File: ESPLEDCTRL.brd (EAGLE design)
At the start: 102.5 x 80 mm, 5 parts, among them J1 22-27-2031-03, X3 ZX62D-B-5PA8

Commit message: Eine Diode
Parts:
- added D1: 1N4148DO35-7, diode:DO35-7
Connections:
- new net N$2: D1.C, U$1.JP2.8
- net VCC: now also D1.A; no longer U$1.JP2.8
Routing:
- net VCC: track 118.5 -> 69.4 mm
- net N$2: track 0.00 -> 49.0 mm
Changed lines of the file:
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@@
 <?xml version="1.0" encoding="utf-8"?>
 <!DOCTYPE eagle SYSTEM "eagle.dtd">
-<eagle version="9.5.1">
+<eagle version="8.7.1">
 <drawing>
 <settings>
@@
 <param name="checkStop" value="0"/>
 <param name="checkValues" value="0"/>
-<param name="checkNames" value="1"/>
-<param name="checkWireStubs" value="1"/>
-<param name="checkPolygonWidth" value="0"/>
 <param name="useDiameter" value="13"/>
 <param name="maxErrors" value="50"/>
@@
 <attribute name="VALUE" x="65.5589" y="59.7169" size="0.8128" layer="27" ratio="10" rot="R90"/>
 </element>
+<element name="D1" library="diode" library_urn="urn:adsk.eagle:library:210" package="DO35-7" package3d_urn="urn:adsk.eagle:package:43339/1" value="1N4148DO35-7" x="6.35" y="-7.62"/>
 </elements>
 <signals>
@@
 <signal name="VCC">
 <contactref element="X3" pad="1"/>
-<contactref element="U$1" pad="JP2.8"/>
 <wire x1="36.2712" y1="62.3316" x2="10.668" y2="62.3316" width="0.1524" layer="1"/>
 <wire x1="10.668" y1="62.3316" x2="8.6868" y2="62.3316" width="0.1524" layer="1"/>
 <wire x1="39.9288" y1="65.9892" x2="36.2712" y2="62.3316" width="0.1524" layer="1"/>
 <wire x1="8.6868" y1="62.3316" x2="8.635" y2="62.26" width="0.1524" layer="1"/>
-<wire x1="39.9288" y1="65.9892" x2="40.005" y2="66.04" width="0.1524" layer="1"/>
-<wire x1="40.0812" y1="65.9892" x2="59.1312" y2="65.9892" width="0.1524" layer="1"/>
-<wire x1="59.1312" y1="65.9892" x2="60.96" y2="65.9892" width="0.1524" layer="1"/>
-<wire x1="40.0812" y1="65.9892" x2="40.005" y2="66.04" width="0.1524" layer="1"/>
 <wire x1="5.334" y1="31.242" x2="7.62" y2="28.956" width="0.1524" layer="1"/>
 <wire x1="5.334" y1="52.2732" x2="5.334" y2="31.242" width="0.1524" layer="1"/>
 <wire x1="10.668" y1="57.6072" x2="5.334" y2="52.2732" width="0.1524" layer="1"/>
 <wire x1="10.668" y1="62.3316" x2="10.668" y2="57.6072" width="0.1524" layer="1"/>
-<wire x1="59.5884" y1="60.0456" x2="59.5884" y2="38.1" width="0.1524" layer="1"/>
-<wire x1="59.1312" y1="60.5028" x2="59.5884" y2="60.0456" width="0.1524" layer="1"/>
-<wire x1="59.1312" y1="65.9892" x2="59.1312" y2="60.5028" width="0.1524" layer="1"/>
-<contactref element="X2" pad="1"/>
 <contactref element="X1" pad="1"/>
 <contactref element="J1" pad="1"/>
-<wire x1="60.96" y1="65.9892" x2="60.96" y2="66.04" width="0" layer="19" extent="1-1"/>
-<wire x1="59.69" y1="38.0746" x2="59.5884" y2="38.1" width="0" layer="19" extent="1-1"/>
+<contactref element="X2" pad="1"/>
+<contactref element="D1" pad="A"/>
+<wire x1="39.9288" y1="65.9892" x2="60.96" y2="66.04" width="0" layer="19" extent="1-1"/>
 <wire x1="7.62" y1="26.6954" x2="7.62" y2="28.956" width="0" layer="19" extent="1-1"/>
+<wire x1="59.69" y1="38.0746" x2="60.96" y2="66.04" width="0" layer="19" extent="1-1"/>
+<wire x1="10.16" y1="-7.62" x2="7.62" y2="26.6954" width="0" layer="19" extent="1-1"/>
 </signal>
 <signal name="N$1">
@@
 <wire x1="60.96" y1="63.5508" x2="60.96" y2="63.5" width="0.1524" layer="16"/>
 </signal>
+<signal name="N$2">
+<contactref element="U$1" pad="JP2.8"/>
+<contactref element="D1" pad="C"/>
+<wire x1="40.0812" y1="65.9892" x2="59.1312" y2="65.9892" width="0.1524" layer="1"/>
+<wire x1="59.1312" y1="65.9892" x2="60.96" y2="65.9892" width="0.1524" layer="1"/>
+<wire x1="40.0812" y1="65.9892" x2="40.005" y2="66.04" width="0.1524" layer="1"/>
+<wire x1="59.5884" y1="60.0456" x2="59.5884" y2="38.1" width="0.1524" layer="1"/>
+<wire x1="59.1312" y1="60.5028" x2="59.5884" y2="60.0456" width="0.1524" layer="1"/>
+<wire x1="59.1312" y1="65.9892" x2="59.1312" y2="60.5028" width="0.1524" layer="1"/>
+<wire x1="2.54" y1="-7.62" x2="59.5884" y2="38.1" width="0" layer="19" extent="1-1"/>
+</signal>
 </signals>
-<mfgpreviewcolors>
-<mfgpreviewcolor name="soldermaskcolor" color="0xC8008000"/>
-<mfgpreviewcolor name="silkscreencolor" color="0xFFFEFEFE"/>
-<mfgpreviewcolor name="backgroundcolor" color="0xFF282828"/>
-<mfgpreviewcolor name="coppercolor" color="0xFFFFBF00"/>
-<mfgpreviewcolor name="substratecolor" color="0xFF786E46"/>
-</mfgpreviewcolors>
 </board>
 </drawing>

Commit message: Die Diode
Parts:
- moved D1 36.6 mm to (26.7, 22.9), turned to 180 degrees
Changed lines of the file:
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@@
 <attribute name="VALUE" x="65.5589" y="59.7169" size="0.8128" layer="27" ratio="10" rot="R90"/>
 </element>
-<element name="D1" library="diode" library_urn="urn:adsk.eagle:library:210" package="DO35-7" package3d_urn="urn:adsk.eagle:package:43339/1" value="1N4148DO35-7" x="6.35" y="-7.62"/>
+<element name="D1" library="diode" library_urn="urn:adsk.eagle:library:210" package="DO35-7" package3d_urn="urn:adsk.eagle:package:43339/1" value="1N4148DO35-7" x="26.67" y="22.86" rot="R180"/>
 </elements>
 <signals>
@@
 <wire x1="7.62" y1="26.6954" x2="7.62" y2="28.956" width="0" layer="19" extent="1-1"/>
 <wire x1="59.69" y1="38.0746" x2="60.96" y2="66.04" width="0" layer="19" extent="1-1"/>
-<wire x1="10.16" y1="-7.62" x2="7.62" y2="26.6954" width="0" layer="19" extent="1-1"/>
+<wire x1="22.86" y1="22.86" x2="7.62" y2="26.6954" width="0" layer="19" extent="1-1"/>
 </signal>
 <signal name="N$1">
@@
 <wire x1="59.1312" y1="60.5028" x2="59.5884" y2="60.0456" width="0.1524" layer="1"/>
 <wire x1="59.1312" y1="65.9892" x2="59.1312" y2="60.5028" width="0.1524" layer="1"/>
-<wire x1="2.54" y1="-7.62" x2="59.5884" y2="38.1" width="0" layer="19" extent="1-1"/>
+<wire x1="30.48" y1="22.86" x2="59.5884" y2="38.1" width="0" layer="19" extent="1-1"/>
 </signal>
 </signals>

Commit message: some changes
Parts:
- moved D1 47.1 mm to (30.5, 69.8)
- moved X1 5.24 mm to (8.89, 34.3)
- moved J1 4.02 mm to (59.7, 59.7)
- moved X2 2.84 mm to (57.1, 34.3)
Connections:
- net VCC renamed N$3
- new net N$4: J1.3, X1.2, X2.2
- net GND: no longer J1.3, X1.2, X2.2, X3.5
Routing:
- net GND: track 146.9 -> 0.00 mm
- net N$4: track 0.00 -> 76.8 mm
- net N$3: track 69.4 -> 115.9 mm
- net N$2: track 49.0 -> 7.33 mm
- net N$1: track 28.0 -> 30.0 mm

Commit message: Alte Version
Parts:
- added J2: 22-27-2041-04, con-molex:6410-04
- added JP1: (no value), jumper:JP5Q
- added S1: (no value), switch-omron:B3F-10XX
- added SV1: (no value), con-lstb:MA03-1
- added X4: MINI-USB-32005-201, con-cypressindustries:32005-201
- moved D1 62.7 mm to (22.9, 7.62), turned to 270 degrees
- moved X2 33.8 mm to (76.2, 6.35), turned to 90 degrees
- moved J1 33.5 mm to (73.7, 29.2)
- moved U$1 32.6 mm to (43.2, 24.1), turned to 270 degrees
- moved X1 28.0 mm to (7.62, 6.35)
- moved X3 26.7 mm to (3.81, 34.3)
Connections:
- removed net 3V3: U$1.JP1.8
- new net N$10: J2.3, U$1.JP1.2
- new net N$11: J1.3, J2.1, JP1.10, JP1.2, JP1.4, JP1.6, JP1.8, S1.3, X1.2, X2.2, X3.5, X4.5
- new net N$12: J2.4, U$1.JP1.8
- new net N$13: D1.A, J1.1, SV1.1, X1.1, X2.1, X3.1, X4.1
- new net N$14: SV1.3, X3.3
- new net N$5: JP1.1, U$1.JP2.4
- new net N$6: J2.2, U$1.JP1.1
- new net N$7: JP1.3, U$1.JP2.3
- new net N$8: JP1.5, U$1.JP2.2
- new net N$9: JP1.7, U$1.JP2.1
- net N$3: now also SV1.2, X3.2; no longer D1.A, J1.1, X1.1, X2.1, X3.1
- net N$4: now also JP1.9, S1.1, U$1.JP2.5; no longer J1.3, X1.2, X2.2
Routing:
- net N$3: track 115.9 -> 0.00 mm
- net N$4: track 76.8 -> 0.00 mm
- net N$1: track 30.0 -> 0.00 mm
- net N$2: track 7.33 -> 0.00 mm
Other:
- board size 102.5 x 80 mm -> 83.5 x 43.2 mm

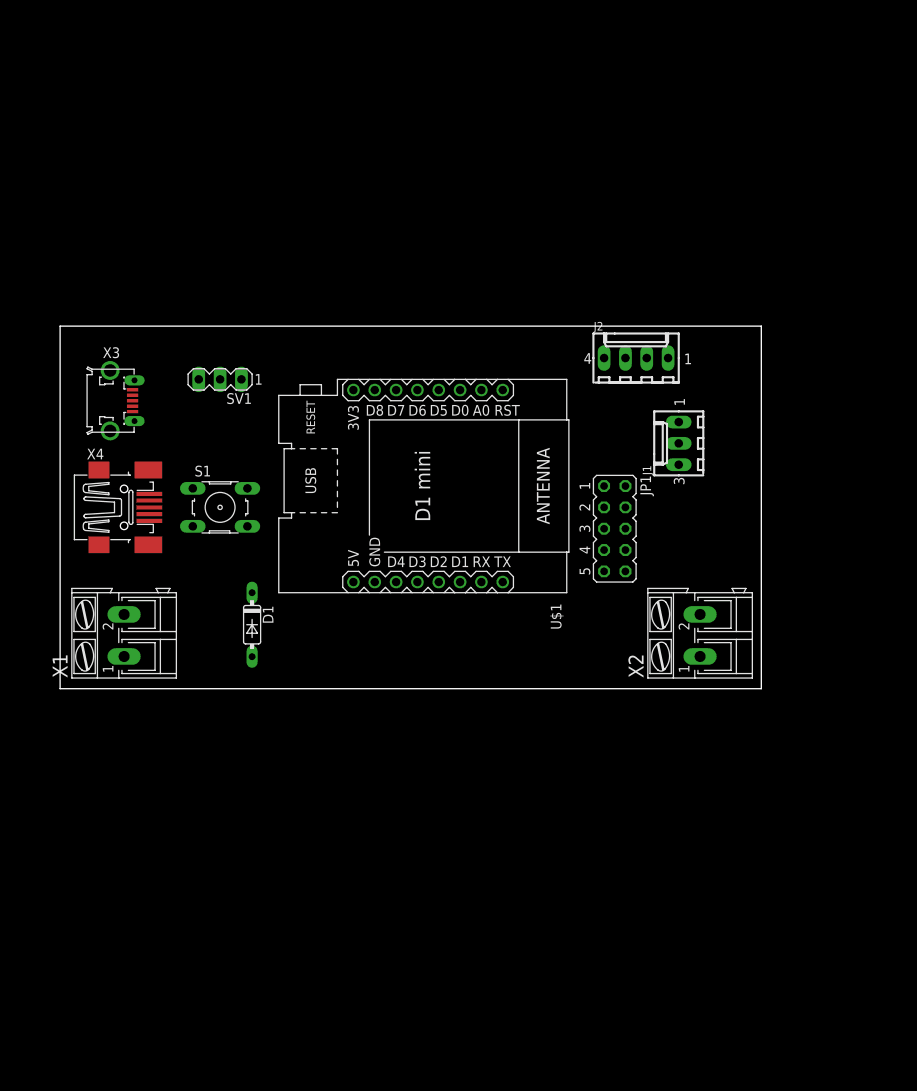
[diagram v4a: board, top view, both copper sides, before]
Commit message: Umbau auf Version 2 beginnt
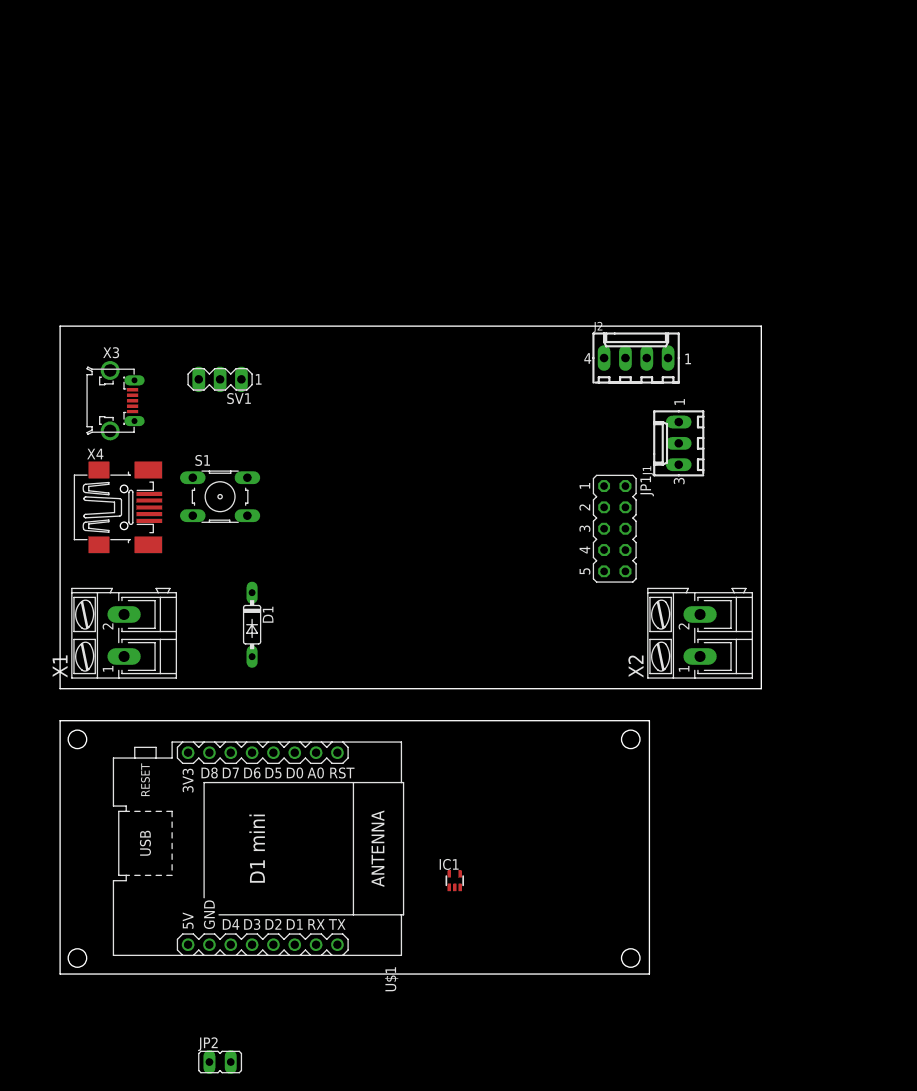
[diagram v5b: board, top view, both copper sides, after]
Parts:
- added IC1: 74HC1G08GW, Logik-IC:SOT353
- added JP2: (no value), jumper:JP1
- moved U$1 47.5 mm to (23.5, -19.1)
- moved S1 1.27 mm to (19.1, 22.9)
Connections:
- new net +5V: IC1.5, U$1.JP2.8
- new net 3V3: U$1.JP1.8
- new net N$15: U$1.JP2.6
- new net N$16: IC1.1, IC1.2, U$1.JP2.2
- new net N$18: IC1.4
- net GND: now also IC1.3, JP2.1
- net N$1: now also JP2.2, U$1.JP2.5; no longer J1.2, U$1.JP2.6
- net N$10: no longer U$1.JP1.2
- net N$12: no longer U$1.JP1.8
- net N$2: no longer U$1.JP2.8
- net N$4: no longer U$1.JP2.5
- net N$5: no longer U$1.JP2.4
- net N$6: no longer U$1.JP1.1
- net N$7: no longer U$1.JP2.3
- net N$8: no longer U$1.JP2.2
- net N$9: no longer U$1.JP2.1
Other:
- board size 83.5 x 43.2 mm -> 83.5 x 77.1 mm

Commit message: Leiterplatte Anordnung vorbereitet DCDC wandler ist 14mm hoch
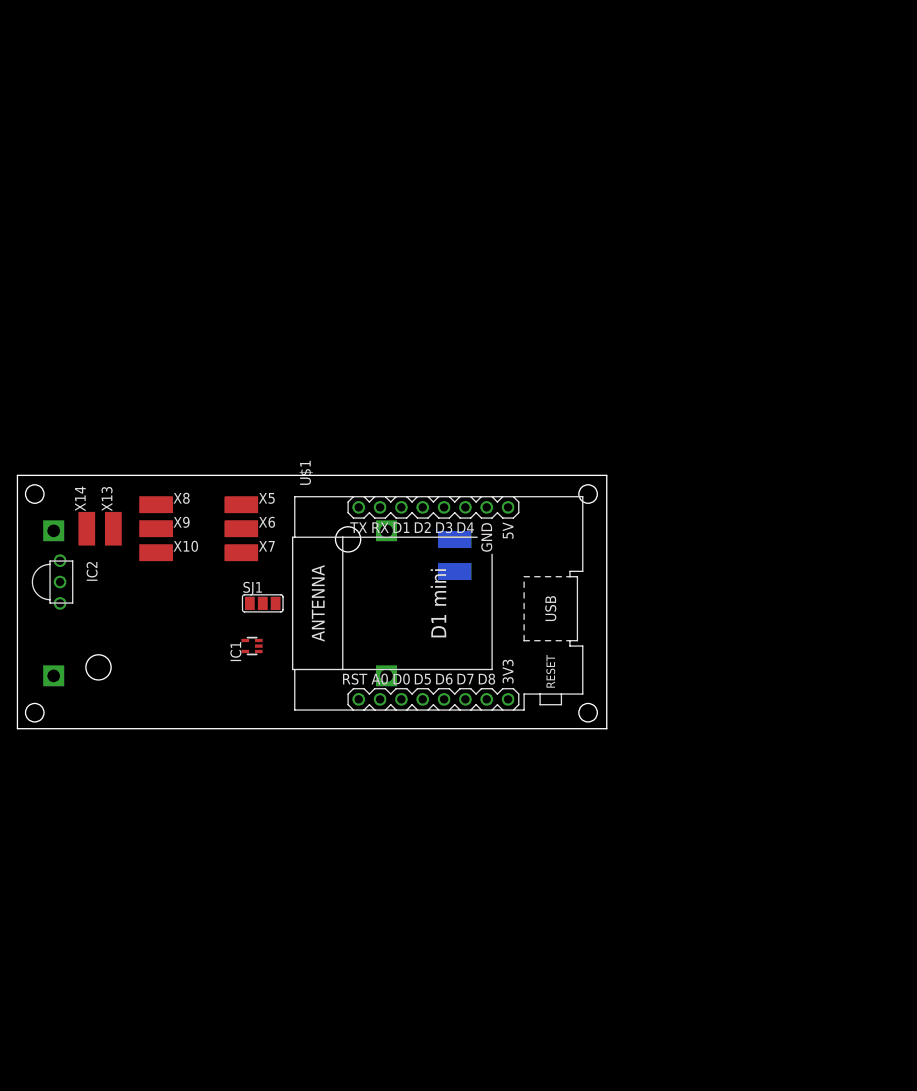
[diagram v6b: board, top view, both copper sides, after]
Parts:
- removed D1: 1N4148DO35-7, diode:DO35-7
- removed J1: 22-27-2031-03, con-molex:6410-03
- removed J2: 22-27-2041-04, con-molex:6410-04
- removed JP1: (no value), jumper:JP5Q
- removed JP2: (no value), jumper:JP1
- removed S1: (no value), switch-omron:B3F-10XX
- removed SV1: (no value), con-lstb:MA03-1
- removed X1, X2: (no value), con-ptr500:AK300/2
- removed X3: ZX62D-B-5PA8, zx62d-b-5pa8-oshpark_10:ZX62D-B-5PA8
- removed X4: MINI-USB-32005-201, con-cypressindustries:32005-201
- added IC2: (no value), modules:TSOP38
- added SJ1: (no value), jumper:SJ_2
- added U$2: DC-DC-STEP-DOWN-LM2596, diy-modules:DC-DC-STEP-DOWN-LM2596
- added X10, X11, X12, X13, X14, X5, X6, X7, X8, X9: (no value), modules:PAD2X4
- moved IC1 36.9 mm to (22.9, 5.08), turned to 90 degrees
- moved U$1 36.3 mm to (45.1, 10.2), turned to 90 degrees
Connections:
- removed net N$10: J2.3
- removed net N$11: J1.3, J2.1, JP1.10, JP1.2, JP1.4, JP1.6, JP1.8, S1.3, X1.2, X2.2, X3.5, X4.5
- removed net N$12: J2.4
- removed net N$13: D1.A, J1.1, SV1.1, X1.1, X2.1, X3.1, X4.1
- removed net N$14: SV1.3, X3.3
- removed net N$3: SV1.2, X3.2
- removed net N$4: JP1.9, S1.1
- removed net N$5: JP1.1
- removed net N$6: J2.2
- removed net N$7: JP1.3
- removed net N$8: JP1.5
- removed net N$9: JP1.7
- new net N$17: SJ1.3, U$1.JP1.3
- new net N$21: U$2.IN+, X11.P$1
- net +5V: now also IC2.3, U$2.OUT+, X5.P$1, X8.P$1
- net GND: now also IC2.2, U$2.IN-, U$2.OUT-, X10.P$1, X12.P$1, X14.P$1, X7.P$1; no longer JP2.1
- net N$1: now also X13.P$1; no longer JP2.2
- net N$15: now also SJ1.1
- net N$16: now also SJ1.2; no longer U$1.JP2.2
- net N$18: now also X6.P$1
- net N$2: now also IC2.1, U$1.JP2.4; no longer D1.C
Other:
- board size 83.5 x 77.1 mm -> 70.2 x 30.2 mm

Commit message: Board fertig gestellt
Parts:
- removed X9: (no value), modules:PAD2X4
- added C1, C2: (no value), rcl:C1206
- added C12: 100uF, rcl:PANASONIC_D
- added D1: 1N5819-T, diode:DO41-7.6
- added SJ2: (no value), jumper:SJ_2
- moved X8 48.9 mm to (59.1, 10.8), flipped to the bottom
- moved X10 47.6 mm to (59.1, 16.5), flipped to the bottom
- moved X5 31.5 mm to (51.1, 10.8), flipped to the bottom
- moved X6 30.0 mm to (51.1, 13.7), flipped to the bottom
- moved X7 29.5 mm to (51.1, 16.5), flipped to the bottom
- moved X12 13.4 mm to (59.1, 19.7)
- moved X11 13.2 mm to (59.1, 23.2)
- moved IC1 10.1 mm to (15.6, 12.1), turned to 270 degrees
- moved SJ1 7.41 mm to (22.9, 17.5), turned to 180 degrees
- moved X14 5.28 mm to (7.62, 16.2)
- moved X13 5.02 mm to (10.5, 16.2)
- moved U$2 2.86 mm to (21.9, 10.2)
- moved IC2 2.03 mm to (-1.27, 14.3)
- moved U$1 0.63 mm to (45.7, 10.2)
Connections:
- removed net N$21: U$2.IN+, X11.P$1
- new net +12V: D1.C, SJ2.1, U$2.IN+, X11.P$1
- new net V+: SJ2.2, X5.P$1, X8.P$1
- net +5V: now also C1.1, C12.+, C2.1, D1.A, SJ2.3; no longer X5.P$1, X8.P$1
- net GND: now also C1.2, C12.-, C2.2
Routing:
- net +12V: track 0.00 -> 205.6 mm, vias 0 -> 1
- net +5V: track 0.00 -> 140.3 mm, vias 0 -> 3
- net GND: track 0.00 -> 92.0 mm, vias 0 -> 11
- net N$2: track 0.00 -> 60.6 mm
- net N$17: track 0.00 -> 50.0 mm
- net N$1: track 0.00 -> 47.2 mm
- net V+: track 0.00 -> 41.8 mm
- net N$18: track 0.00 -> 41.7 mm, vias 0 -> 1
- net N$15: track 0.00 -> 32.4 mm
- net N$16: track 0.00 -> 15.7 mm
- added copper zone on layer 1, net GND
- added copper zone on layer 16, net GND
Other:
- board text added: "+"
- board text added: "12"
- board text added: "16"
- board text added: "2"
- board text added: "5"
- board text added: "G"
- board text added: "LED S"
- board text added: "PB"
